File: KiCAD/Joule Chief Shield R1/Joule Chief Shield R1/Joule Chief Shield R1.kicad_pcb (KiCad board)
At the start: 2 copper layers, 68.6 x 53.3 mm, 8 parts, among them J1 Power, J2 Digital/PWM, J3 Analog, J4 Digital/PWM

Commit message: ERC+prep for board layout
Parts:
- added C1: 0.1u, Capacitor_SMD:C_0805_2012Metric_Pad1.18x1.45mm_HandSolder, F.Cu at (252.9, 90.4)
- added C10: 0.1u, Capacitor_SMD:C_0805_2012Metric_Pad1.18x1.45mm_HandSolder, F.Cu at (257.7, 90.4)
- added C11: 0.1u, Capacitor_SMD:C_0805_2012Metric_Pad1.18x1.45mm_HandSolder, F.Cu at (257.7, 93.4)
- added C12: 0.1u, Capacitor_SMD:C_0805_2012Metric_Pad1.18x1.45mm_HandSolder, F.Cu at (257.7, 96.4)
- added C13: 0.1u, Capacitor_SMD:C_0805_2012Metric_Pad1.18x1.45mm_HandSolder, F.Cu at (257.7, 99.4)
- added C14: 10u, Capacitor_SMD:C_0805_2012Metric_Pad1.18x1.45mm_HandSolder, F.Cu at (257.7, 102.4)
- added C2: 1F, 000_Dropbin:1F_Supercap, F.Cu at (204.6, 75.1)
- added C3: 0.1u, Capacitor_SMD:C_0805_2012Metric_Pad1.18x1.45mm_HandSolder, F.Cu at (252.9, 93.4)
- added C4: 100u, Capacitor_THT:CP_Radial_D5.0mm_P2.00mm, F.Cu at (243.3, 110.4)
- added C5: 1F, 000_Dropbin:1F_Supercap, F.Cu at (216.7, 75.1)
- added C6: 10u, Capacitor_SMD:C_0805_2012Metric_Pad1.18x1.45mm_HandSolder, F.Cu at (252.9, 96.4)
- added C7: 1u, Capacitor_SMD:C_0805_2012Metric_Pad1.18x1.45mm_HandSolder, F.Cu at (252.9, 99.4)
- added C8: 4.7u, Capacitor_SMD:C_0805_2012Metric_Pad1.18x1.45mm_HandSolder, F.Cu at (252.9, 102.4)
- added C9: 0.1u, Capacitor_SMD:C_0805_2012Metric_Pad1.18x1.45mm_HandSolder, F.Cu at (252.9, 105.4)
- added D1: LED, LED_SMD:LED_0805_2012Metric_Pad1.15x1.40mm_HandSolder, F.Cu at (243.3, 90.4)
- added D10: LED, LED_SMD:LED_0805_2012Metric_Pad1.15x1.40mm_HandSolder, F.Cu at (248.1, 99.5)
- added D11: LED, LED_SMD:LED_0805_2012Metric_Pad1.15x1.40mm_HandSolder, F.Cu at (248.1, 102.5)
- added D2: LED, LED_SMD:LED_0805_2012Metric_Pad1.15x1.40mm_HandSolder, F.Cu at (243.3, 93.4)
- added D3: LED, LED_SMD:LED_0805_2012Metric_Pad1.15x1.40mm_HandSolder, F.Cu at (243.3, 96.5)
- added D4: LED, LED_SMD:LED_0805_2012Metric_Pad1.15x1.40mm_HandSolder, F.Cu at (243.3, 99.5)
- added D5: LED, LED_SMD:LED_0805_2012Metric_Pad1.15x1.40mm_HandSolder, F.Cu at (243.3, 102.5)
- added D6: LED, LED_SMD:LED_0805_2012Metric_Pad1.15x1.40mm_HandSolder, F.Cu at (243.3, 105.6)
- added D7: LED, LED_SMD:LED_0805_2012Metric_Pad1.15x1.40mm_HandSolder, F.Cu at (248.1, 90.4)
- added D8: LED, LED_SMD:LED_0805_2012Metric_Pad1.15x1.40mm_HandSolder, F.Cu at (248.1, 93.4)
- added D9: LED, LED_SMD:LED_0805_2012Metric_Pad1.15x1.40mm_HandSolder, F.Cu at (248.1, 96.5)
- added J1: Conn_01x06, Connector_JST:JST_PH_B7B-PH-K_1x07_P2.00mm_Vertical, F.Cu at (183.6, 64.3)
- added J2: Conn_01x06, Connector_JST:JST_PH_B7B-PH-K_1x07_P2.00mm_Vertical, F.Cu at (183.6, 70.9)
- added J3: Conn_01x06, Connector_JST:JST_PH_B7B-PH-K_1x07_P2.00mm_Vertical, F.Cu at (183.6, 77.4)
- added J4: Conn_01x06, Connector_JST:JST_PH_B7B-PH-K_1x07_P2.00mm_Vertical, F.Cu at (183.6, 84.0)
- added J5: Conn_01x06, Connector_JST:JST_PH_B7B-PH-K_1x07_P2.00mm_Vertical, F.Cu at (183.6, 90.5)
- added J6: Conn_01x06, Connector_JST:JST_PH_B7B-PH-K_1x07_P2.00mm_Vertical, F.Cu at (183.6, 97.1)
- added J7: Conn_01x06, Connector_JST:JST_PH_B7B-PH-K_1x07_P2.00mm_Vertical, F.Cu at (183.6, 103.6)
- added JP1: SolderJumper_2_Open, Jumper:SolderJumper-2_P1.3mm_Open_RoundedPad1.0x1.5mm, F.Cu at (224.9, 63.4)
- added JP10: SolderJumper_2_Open, Jumper:SolderJumper-2_P1.3mm_Open_RoundedPad1.0x1.5mm, F.Cu at (233.6, 66.9)
- added JP11: SolderJumper_2_Open, Jumper:SolderJumper-2_P1.3mm_Open_RoundedPad1.0x1.5mm, F.Cu at (233.6, 70.5)
- added JP12: SolderJumper_2_Open, Jumper:SolderJumper-2_P1.3mm_Open_RoundedPad1.0x1.5mm, F.Cu at (233.6, 74.0)
- added JP13: SolderJumper_2_Open, Jumper:SolderJumper-2_P1.3mm_Open_RoundedPad1.0x1.5mm, F.Cu at (237.9, 63.4)
- added JP14: SolderJumper_2_Open, Jumper:SolderJumper-2_P1.3mm_Open_RoundedPad1.0x1.5mm, F.Cu at (237.9, 66.9)
- added JP15: SolderJumper_2_Open, Jumper:SolderJumper-2_P1.3mm_Open_RoundedPad1.0x1.5mm, F.Cu at (237.9, 70.5)
- added JP16: SolderJumper_2_Open, Jumper:SolderJumper-2_P1.3mm_Open_RoundedPad1.0x1.5mm, F.Cu at (237.9, 74.0)
- added JP17: SolderJumper_2_Open, Jumper:SolderJumper-2_P1.3mm_Open_RoundedPad1.0x1.5mm, F.Cu at (242.3, 63.4)
- added JP18: SolderJumper_2_Open, Jumper:SolderJumper-2_P1.3mm_Open_RoundedPad1.0x1.5mm, F.Cu at (242.3, 66.9)
- added JP19: SolderJumper_2_Open, Jumper:SolderJumper-2_P1.3mm_Open_RoundedPad1.0x1.5mm, F.Cu at (242.3, 70.5)
- added JP2: SolderJumper_2_Open, Jumper:SolderJumper-2_P1.3mm_Open_RoundedPad1.0x1.5mm, F.Cu at (224.9, 66.9)
- added JP20: SolderJumper_2_Open, Jumper:SolderJumper-2_P1.3mm_Open_RoundedPad1.0x1.5mm, F.Cu at (242.3, 74.0)
- added JP3: SolderJumper_2_Open, Jumper:SolderJumper-2_P1.3mm_Open_RoundedPad1.0x1.5mm, F.Cu at (224.9, 70.5)
- added JP4: SolderJumper_2_Open, Jumper:SolderJumper-2_P1.3mm_Open_RoundedPad1.0x1.5mm, F.Cu at (224.9, 74.0)
- added JP5: SolderJumper_2_Open, Jumper:SolderJumper-2_P1.3mm_Open_RoundedPad1.0x1.5mm, F.Cu at (229.2, 63.4)
- added JP6: SolderJumper_2_Open, Jumper:SolderJumper-2_P1.3mm_Open_RoundedPad1.0x1.5mm, F.Cu at (229.2, 66.9)
- added JP7: SolderJumper_2_Open, Jumper:SolderJumper-2_P1.3mm_Open_RoundedPad1.0x1.5mm, F.Cu at (229.2, 70.5)
- added JP8: SolderJumper_2_Open, Jumper:SolderJumper-2_P1.3mm_Open_RoundedPad1.0x1.5mm, F.Cu at (229.2, 74.0)
- added JP9: SolderJumper_2_Open, Jumper:SolderJumper-2_P1.3mm_Open_RoundedPad1.0x1.5mm, F.Cu at (233.6, 63.4)
- added L1: 10u, 000_Dropbin:Power_Inductor_101040, F.Cu at (248.4, 82.3)
- added LITH1: 18650, 000_Dropbin:18650_Cell_Clip_V2, F.Cu at (220.7, 50.1)
- added Q1: AO3400A, Package_TO_SOT_SMD:SOT-23, F.Cu at (225.1, 78.2)
- added Q10: AO3400A, Package_TO_SOT_SMD:SOT-23, F.Cu at (230.0, 96.7)
- added Q2: AO3400A, Package_TO_SOT_SMD:SOT-23, F.Cu at (225.1, 82.8)
- added Q3: AO3400A, Package_TO_SOT_SMD:SOT-23, F.Cu at (225.1, 87.5)
- added Q4: AO3400A, Package_TO_SOT_SMD:SOT-23, F.Cu at (225.1, 92.1)
- added Q5: AO3400A, Package_TO_SOT_SMD:SOT-23, F.Cu at (225.1, 96.7)
- added Q6: AO3400A, Package_TO_SOT_SMD:SOT-23, F.Cu at (230.0, 78.2)
- added Q7: AO3400A, Package_TO_SOT_SMD:SOT-23, F.Cu at (230.0, 82.8)
- added Q8: AO3400A, Package_TO_SOT_SMD:SOT-23, F.Cu at (230.0, 87.5)
- added Q9: AO3400A, Package_TO_SOT_SMD:SOT-23, F.Cu at (230.0, 92.1)
- added R1: 0.1R, Resistor_SMD:R_Shunt_Vishay_WSK2512_6332Metric_T1.19mm, F.Cu at (249.3, 64.0)
- added R10: 1k, Resistor_SMD:R_0805_2012Metric_Pad1.20x1.40mm_HandSolder, F.Cu at (201.0, 110.8)
- added R11: 1k, Resistor_SMD:R_0805_2012Metric_Pad1.20x1.40mm_HandSolder, F.Cu at (201.0, 113.7)
- added R12: 1k, Resistor_SMD:R_0805_2012Metric_Pad1.20x1.40mm_HandSolder, F.Cu at (205.7, 90.1)
- added R13: 1k, Resistor_SMD:R_0805_2012Metric_Pad1.20x1.40mm_HandSolder, F.Cu at (205.7, 93.1)
- added R14: 10k, Resistor_SMD:R_0805_2012Metric_Pad1.20x1.40mm_HandSolder, F.Cu at (205.7, 96.0)
- added R15: 2k2, Resistor_SMD:R_0805_2012Metric_Pad1.20x1.40mm_HandSolder, F.Cu at (205.7, 99.0)
- added R16: 2k2, Resistor_SMD:R_0805_2012Metric_Pad1.20x1.40mm_HandSolder, F.Cu at (205.7, 101.9)
- added R17: 1K, Resistor_SMD:R_0805_2012Metric_Pad1.20x1.40mm_HandSolder, F.Cu at (205.7, 104.9)
- added R18: 1K, Resistor_SMD:R_0805_2012Metric_Pad1.20x1.40mm_HandSolder, F.Cu at (205.7, 107.8)
- added R19: 1K, Resistor_SMD:R_0805_2012Metric_Pad1.20x1.40mm_HandSolder, F.Cu at (205.7, 110.8)
- added R2: 10, Resistor_SMD:R_0805_2012Metric_Pad1.20x1.40mm_HandSolder, F.Cu at (201.0, 90.1)
- added R20: 1K, Resistor_SMD:R_0805_2012Metric_Pad1.20x1.40mm_HandSolder, F.Cu at (205.7, 113.7)
- added R21: 1K, Resistor_SMD:R_0805_2012Metric_Pad1.20x1.40mm_HandSolder, F.Cu at (210.5, 90.1)
- added R22: 1K, Resistor_SMD:R_0805_2012Metric_Pad1.20x1.40mm_HandSolder, F.Cu at (210.5, 93.1)
- added R23: 1K, Resistor_SMD:R_0805_2012Metric_Pad1.20x1.40mm_HandSolder, F.Cu at (210.5, 96.0)
- added R24: 1K, Resistor_SMD:R_0805_2012Metric_Pad1.20x1.40mm_HandSolder, F.Cu at (210.5, 99.0)
- added R25: 1K, Resistor_SMD:R_0805_2012Metric_Pad1.20x1.40mm_HandSolder, F.Cu at (210.5, 101.9)
- added R26: 10k, Resistor_SMD:R_0805_2012Metric_Pad1.20x1.40mm_HandSolder, F.Cu at (210.5, 104.9)
- added R27: 10k, Resistor_SMD:R_0805_2012Metric_Pad1.20x1.40mm_HandSolder, F.Cu at (210.5, 107.8)
- added R28: 10k, Resistor_SMD:R_0805_2012Metric_Pad1.20x1.40mm_HandSolder, F.Cu at (210.5, 110.8)
- added R29: 10k, Resistor_SMD:R_0805_2012Metric_Pad1.20x1.40mm_HandSolder, F.Cu at (210.5, 113.7)
- added R3: 10, Resistor_SMD:R_0805_2012Metric_Pad1.20x1.40mm_HandSolder, F.Cu at (201.0, 93.1)
- added R30: 10k, Resistor_SMD:R_0805_2012Metric_Pad1.20x1.40mm_HandSolder, F.Cu at (215.2, 90.1)
- added R31: 10k, Resistor_SMD:R_0805_2012Metric_Pad1.20x1.40mm_HandSolder, F.Cu at (215.2, 93.1)
- added R32: 10k, Resistor_SMD:R_0805_2012Metric_Pad1.20x1.40mm_HandSolder, F.Cu at (215.2, 96.0)
- added R33: 10k, Resistor_SMD:R_0805_2012Metric_Pad1.20x1.40mm_HandSolder, F.Cu at (215.2, 99.0)
- added R34: 10k, Resistor_SMD:R_0805_2012Metric_Pad1.20x1.40mm_HandSolder, F.Cu at (215.2, 101.9)
- added R4: 1M, Resistor_SMD:R_0805_2012Metric_Pad1.20x1.40mm_HandSolder, F.Cu at (201.0, 96.0)
- added R5: 220k, Resistor_SMD:R_0805_2012Metric_Pad1.20x1.40mm_HandSolder, F.Cu at (201.0, 99.0)
- added R6: 0.1R, Resistor_SMD:R_Shunt_Vishay_WSK2512_6332Metric_T1.19mm, F.Cu at (249.3, 68.9)
- added R7: 10, Resistor_SMD:R_0805_2012Metric_Pad1.20x1.40mm_HandSolder, F.Cu at (201.0, 101.9)
- added R8: 10, Resistor_SMD:R_0805_2012Metric_Pad1.20x1.40mm_HandSolder, F.Cu at (201.0, 104.9)
- added R9: 100, Resistor_SMD:R_0805_2012Metric_Pad1.20x1.40mm_HandSolder, F.Cu at (201.0, 107.8)
- added TPx1: TestPoint_Alt, TestPoint:TestPoint_THTPad_1.0x1.0mm_Drill0.5mm, F.Cu at (234.0, 102.8)
- added U1: INA219AxD, Package_SO:SOIC-8_3.9x4.9mm_P1.27mm, F.Cu at (236.7, 79.2)
- added U2: LTC3105xMS, Package_SO:MSOP-12_3x4.039mm_P0.65mm, F.Cu at (236.1, 98.5)
- added U3: AD5280, Package_SO:TSSOP-14_4.4x5mm_P0.65mm, F.Cu at (254.9, 110.2)
- added U4: INA219AxD, Package_SO:SOIC-8_3.9x4.9mm_P1.27mm, F.Cu at (236.7, 85.7)
- added U5: DW01, Package_TO_SOT_SMD:SOT-23-6_Handsoldering, F.Cu at (257.2, 64.1)
- added U6: TP4056, Package_SO:SOIC-8-1EP_3.9x4.9mm_P1.27mm_EP2.29x3mm, F.Cu at (236.7, 92.3)
- added U7: FS8205A, Package_TO_SOT_SMD:SOT-23-6_Handsoldering, F.Cu at (257.2, 68.8)
- renumbered J3 to J10, J4 to J11, J2 to J8, J1 to J9
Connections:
- net /SCL/A5 renamed SCL
- net /SDA/A4 renamed SDA
- net VCC renamed VIN
- J11 pad 1: /7 -> SHDN_5
- J11 pad 2: /*6 -> SHDN_6
- J11 pad 3: /*5 -> SHDN_7
- J8 pad 10: /8 -> SHDN_4
- J8 pad 5: /13 -> !BOOST
- J8 pad 6: /12 -> CHARGER
- J8 pad 7: /*11 -> SHDN_1
- J8 pad 8: /*10 -> SHDN_2
- J8 pad 9: /*9 -> SHDN_3
- J9 pad 5: +5V -> VBUS

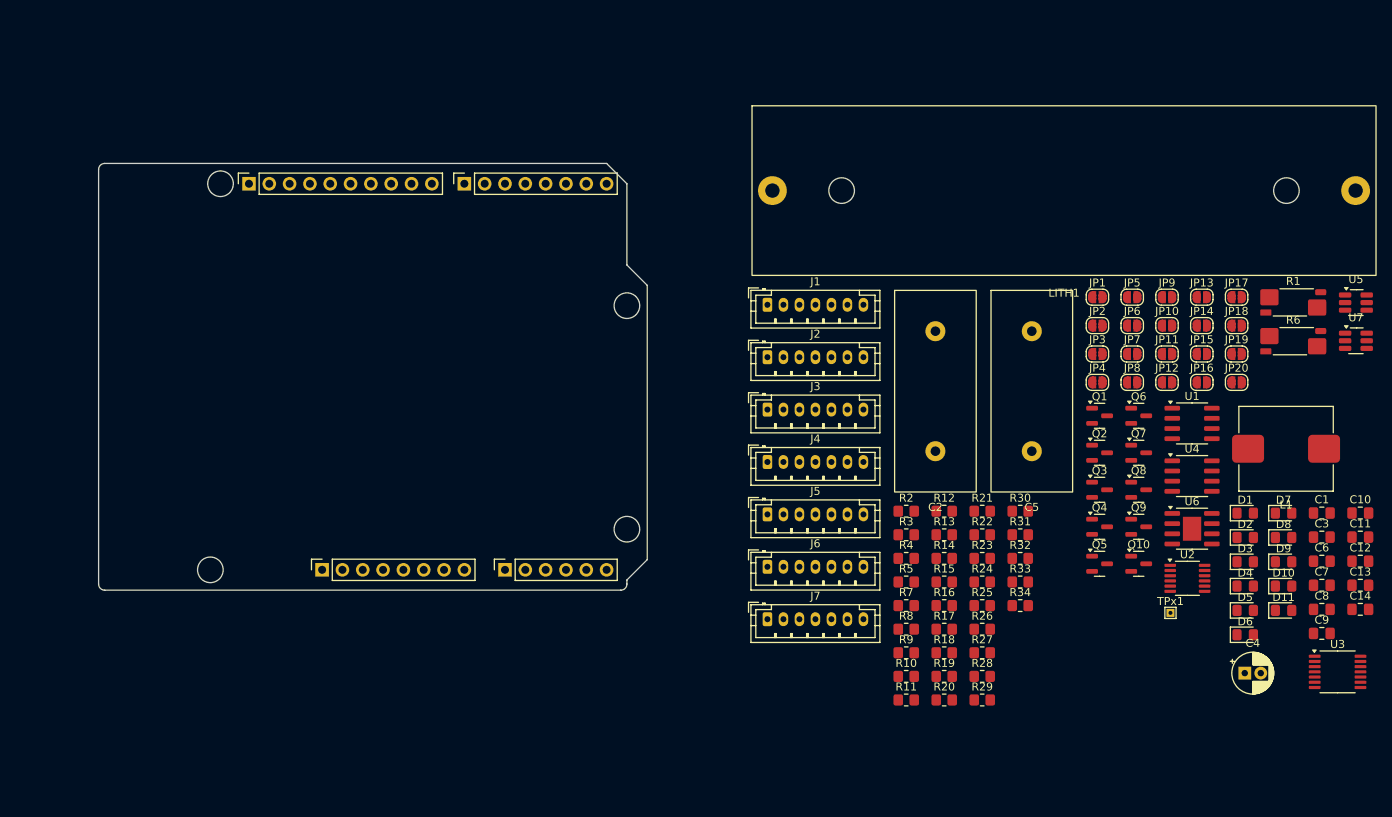
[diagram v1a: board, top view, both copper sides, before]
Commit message: layout extraction module
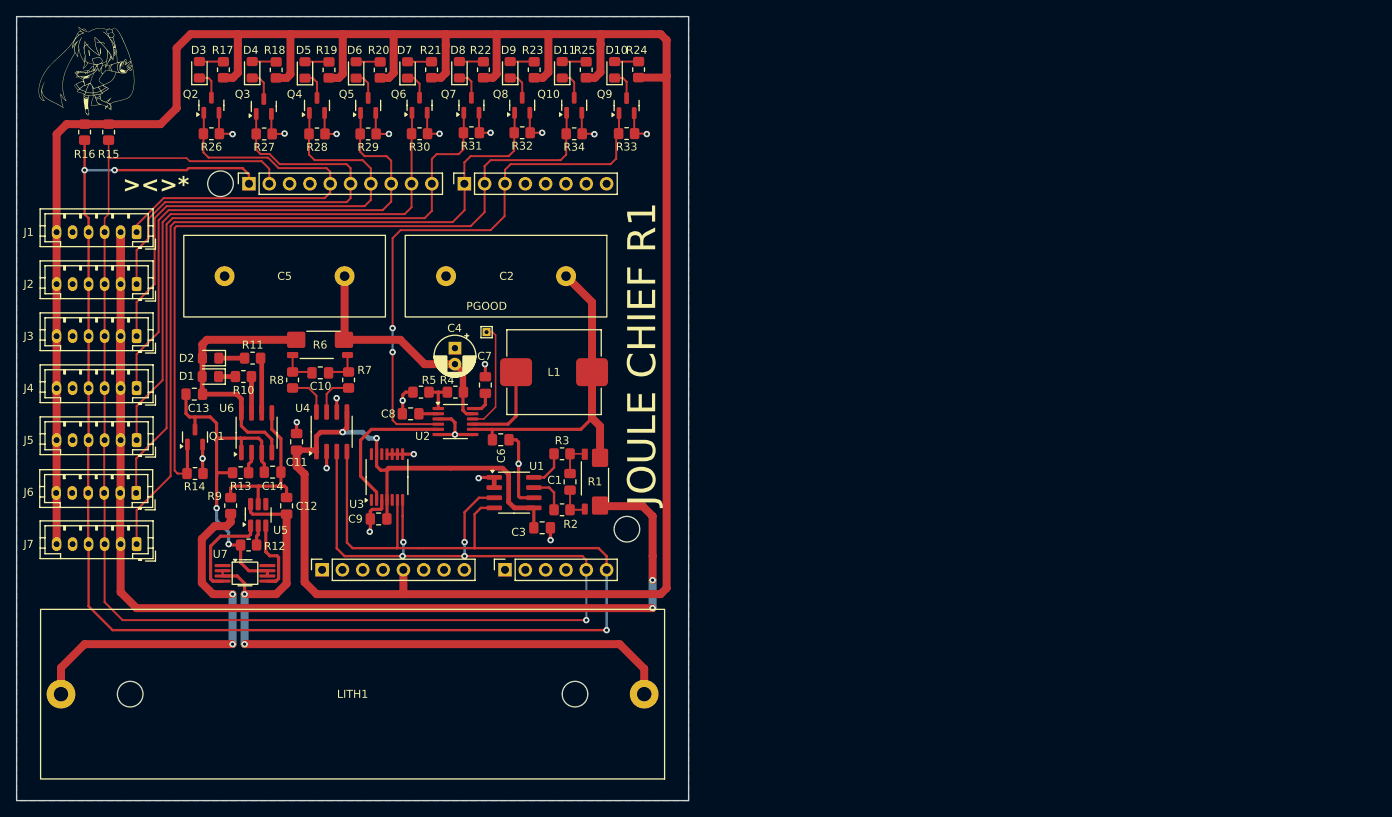
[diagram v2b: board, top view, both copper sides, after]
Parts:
- removed JP1, JP10, JP11, JP12, JP13, JP14, JP15, JP16, JP17, JP18, JP19, JP2, JP20, JP3, JP4, JP5, JP6, JP7, JP8, JP9: SolderJumper_2_Open, Jumper:SolderJumper-2_P1.3mm_Open_RoundedPad1.0x1.5mm
- removed MH2, MH3: MountingHole_3.2mm, Arduino_MountingHole:MountingHole_3.2mm
- added G***: LOGO, LOGO, F.Cu at (100.0, 35.2)
- J1, J2, J3, J4, J5, J6, J7: footprint Connector_JST:JST_PH_B7B-PH-K_1x07_P2.00mm_Vertical -> Connector_JST:JST_PH_B6B-PH-K_1x06_P2.00mm_Vertical
- R1, R6: footprint Resistor_SMD:R_Shunt_Vishay_WSK2512_6332Metric_T1.19mm -> 000_Dropbin:R_Shunt_2512_V2
- U7: footprint Package_TO_SOT_SMD:SOT-23-6_Handsoldering -> 000_Dropbin:FS8205A
- moved C13 147.7 mm to (112.0, 75.5)
- moved D3 144.5 mm to (112.6, 35.0), turned to 90 degrees
- moved U7 141.9 mm to (118.3, 97.9)
- moved D4 139.9 mm to (119.2, 34.9), turned to 90 degrees
- moved U5 139.8 mm to (120.0, 90.6), turned to 90 degrees
- moved C14 137.0 mm to (121.8, 85.2)
- moved D5 135.6 mm to (125.8, 35.0), turned to 90 degrees
- moved C12 134.4 mm to (123.5, 89.5), turned to 90 degrees
- moved C11 133.5 mm to (124.8, 81.5), turned to 90 degrees
- moved D6 131.7 mm to (132.2, 35.0), turned to 90 degrees
- moved D2 131.3 mm to (114.0, 71.0), turned to 180 degrees
- moved C10 131.2 mm to (127.7, 72.8)
- moved D1 130.5 mm to (114.0, 73.3), turned to 180 degrees
- moved D7 122.7 mm to (138.6, 35.0), turned to 90 degrees
- moved R16 122.7 mm to (98.2, 42.8), turned to 90 degrees
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- renumbered TPx1 to PGOOD
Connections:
- J1 pad 1: VBUS -> SHDN_1
- J1 pad 2: GND -> VOUT_1
- J1 pad 5: SHDN_1 -> GND
- J1 pad 6: VOUT_1 -> VBUS
- J11 pad 1: SHDN_5 -> SHDN_7
- J11 pad 2: SHDN_6 -> CHARGER
- J11 pad 3: SHDN_7 -> !BOOST
- J2 pad 1: VBUS -> SHDN_2
- J2 pad 2: GND -> VOUT_1
- J2 pad 5: SHDN_2 -> GND
- J2 pad 6: VOUT_1 -> VBUS
- J3 pad 1: VBUS -> SHDN_3
- J3 pad 2: GND -> VOUT_1
- J3 pad 5: SHDN_3 -> GND
- J3 pad 6: VOUT_1 -> VBUS
- J4 pad 1: VBUS -> SHDN_4
- J4 pad 2: GND -> VOUT_1
- J4 pad 5: SHDN_4 -> GND
- J4 pad 6: VOUT_1 -> VBUS
- J5 pad 1: VBUS -> SHDN_5
- J5 pad 2: GND -> VOUT_1
- J5 pad 5: SHDN_5 -> GND
- J5 pad 6: VOUT_1 -> VBUS
- J6 pad 1: VBUS -> SHDN_6
- J6 pad 2: GND -> VOUT_1
- J6 pad 5: SHDN_6 -> GND
- J6 pad 6: VOUT_1 -> VBUS
- J7 pad 1: VBUS -> SHDN_7
- J7 pad 2: GND -> VOUT_1
- J7 pad 5: SHDN_7 -> GND
- J7 pad 6: VOUT_1 -> VBUS
- J8 pad 10: SHDN_4 -> SHDN_6
- J8 pad 5: !BOOST -> SHDN_1
- J8 pad 6: CHARGER -> SHDN_2
- J8 pad 7: SHDN_1 -> SHDN_3
- J8 pad 8: SHDN_2 -> SHDN_4
- J8 pad 9: SHDN_3 -> SHDN_5
- U1 pad 1: Net-(JP5-A) -> GND
- U1 pad 2: Net-(JP1-A) -> GND
- U3 pad 8: Net-(JP10-A) -> GND
- U3 pad 9: Net-(JP11-A) -> GND
- U4 pad 1: Net-(JP17-A) -> VBUS
- U4 pad 2: Net-(JP13-A) -> GND
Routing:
- net VBUS: track 0.00 -> 447.0 mm, vias 0 -> 2
- net SCL: track 0.00 -> 213.5 mm, vias 0 -> 3
- net SDA: track 0.00 -> 210.4 mm, vias 0 -> 5
- net VOUT_1: track 0.00 -> 157.2 mm, vias 0 -> 2
- net SHDN_7: track 0.00 -> 97.0 mm
- net CHARGER: track 0.00 -> 96.6 mm
- net BAT-: track 0.00 -> 85.9 mm, vias 0 -> 2
- net SHDN_6: track 0.00 -> 84.6 mm
- net GND: track 0.00 -> 83.9 mm, vias 0 -> 21
- net SHDN_5: track 0.00 -> 72.3 mm
- net !BOOST: track 0.00 -> 70.0 mm, vias 0 -> 2
- net SHDN_4: track 0.00 -> 66.5 mm
- net SHDN_3: track 0.00 -> 61.3 mm
- net SHDN_2: track 0.00 -> 56.1 mm
- net SHDN_1: track 0.00 -> 51.2 mm
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- added copper zone on B.Cu, net GND
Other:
- board size 68.6 x 53.3 mm -> 84 x 98 mm
- board text added: "><>*"
- board text added: "JOULE CHIEF R1"
